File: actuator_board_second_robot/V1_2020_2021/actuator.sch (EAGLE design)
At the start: 26 parts, among them CON1 SM03B-GHS-TB, CON2 SM03B-GHS-TB, CON3 MOLEX_5566-2, U3 TCAN1042HVDR, U4 PCA9685PW, U5 TEENSY_3.1_BASIC_2

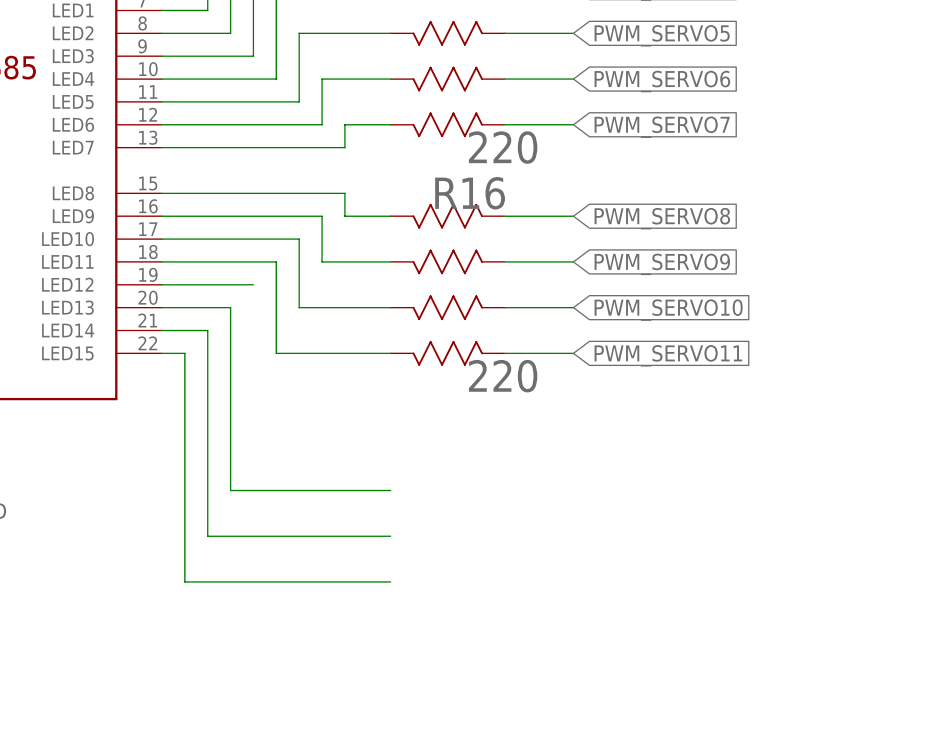
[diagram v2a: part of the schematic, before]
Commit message: Routed some airwires, removed fixed network resistor.
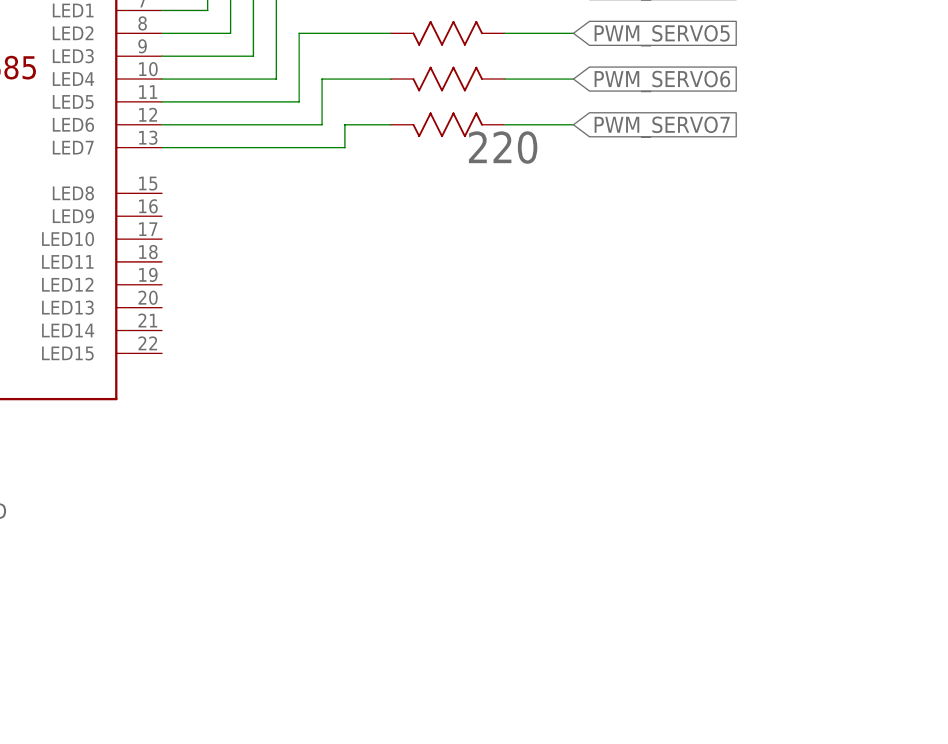
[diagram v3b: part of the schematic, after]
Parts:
- removed R16: 220, ARVP:EXB-V8V221JVEXBV8V-M
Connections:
- removed net N$1: U4.LED12
- removed net PWM_CH10: R16.66, U4.LED10
- removed net PWM_CH11: R16.58, U4.LED11
- removed net PWM_CH13: U4.LED13
- removed net PWM_CH14: U4.LED14
- removed net PWM_CH15: U4.LED15
- removed net PWM_CH8: R16.82, U4.LED8
- removed net PWM_CH9: R16.74, U4.LED9
- removed net PWM_SERVO10: R16.35
- removed net PWM_SERVO11: R16.47
- removed net PWM_SERVO8: R16.11
- removed net PWM_SERVO9: R16.23
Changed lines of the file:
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@@
 <part name="R14" library="ARVP" deviceset="EXB-V8V221JV" device="EXBV8V-M" value="220"/>
 <part name="R15" library="ARVP" deviceset="EXB-V8V221JV" device="EXBV8V-M" value="220"/>
-<part name="R16" library="ARVP" deviceset="EXB-V8V221JV" device="EXBV8V-M" value="220"/>
 <part name="R26" library="ARVP" deviceset="EXB-V8V221JV" device="EXBV8V-M" value="10k"/>
 <part name="SUPPLY10" library="supply2" library_urn="urn:adsk.eagle:library:372" deviceset="GND" device=""/>
@@
 <attribute name="NAME" x="147.5994" y="224.3328" size="3.4798" layer="95" ratio="10" rot="SMR0"/>
 </instance>
-<instance part="R16" gate="A" x="147.32" y="198.12" smashed="yes" rot="MR0">
-<attribute name="VALUE" x="151.2062" y="178.6128" size="3.4798" layer="96" ratio="10" rot="SMR0"/>
-<attribute name="NAME" x="147.5994" y="198.9328" size="3.4798" layer="95" ratio="10" rot="SMR0"/>
-</instance>
 <instance part="R26" gate="A" x="22.86" y="147.32" smashed="yes" rot="R90">
 <attribute name="NAME" x="22.0472" y="147.0406" size="3.4798" layer="95" ratio="10" rot="SR90"/>
@@
 </segment>
 </net>
-<net name="PWM_CH8" class="0">
-<segment>
-<pinref part="U4" gate="G$1" pin="LED8"/>
-<wire x1="109.22" y1="200.66" x2="129.54" y2="200.66" width="0.1524" layer="91"/>
-<wire x1="129.54" y1="200.66" x2="129.54" y2="198.12" width="0.1524" layer="91"/>
-<pinref part="R16" gate="A" pin="82"/>
-<wire x1="129.54" y1="198.12" x2="134.62" y2="198.12" width="0.1524" layer="91"/>
-</segment>
-</net>
-<net name="PWM_CH9" class="0">
-<segment>
-<pinref part="U4" gate="G$1" pin="LED9"/>
-<wire x1="109.22" y1="198.12" x2="127" y2="198.12" width="0.1524" layer="91"/>
-<wire x1="127" y1="198.12" x2="127" y2="193.04" width="0.1524" layer="91"/>
-<wire x1="127" y1="193.04" x2="134.62" y2="193.04" width="0.1524" layer="91"/>
-<pinref part="R16" gate="A" pin="74"/>
-</segment>
-</net>
-<net name="PWM_CH10" class="0">
-<segment>
-<wire x1="124.46" y1="187.96" x2="124.46" y2="195.58" width="0.1524" layer="91"/>
-<pinref part="U4" gate="G$1" pin="LED10"/>
-<wire x1="124.46" y1="195.58" x2="109.22" y2="195.58" width="0.1524" layer="91"/>
-<pinref part="R16" gate="A" pin="66"/>
-<wire x1="124.46" y1="187.96" x2="134.62" y2="187.96" width="0.1524" layer="91"/>
-</segment>
-</net>
-<net name="PWM_CH11" class="0">
-<segment>
-<pinref part="U4" gate="G$1" pin="LED11"/>
-<wire x1="109.22" y1="193.04" x2="121.92" y2="193.04" width="0.1524" layer="91"/>
-<wire x1="121.92" y1="193.04" x2="121.92" y2="182.88" width="0.1524" layer="91"/>
-<pinref part="R16" gate="A" pin="58"/>
-<wire x1="121.92" y1="182.88" x2="134.62" y2="182.88" width="0.1524" layer="91"/>
-</segment>
-</net>
-<net name="PWM_CH13" class="0">
-<segment>
-<wire x1="116.84" y1="167.64" x2="116.84" y2="187.96" width="0.1524" layer="91"/>
-<pinref part="U4" gate="G$1" pin="LED13"/>
-<wire x1="116.84" y1="187.96" x2="109.22" y2="187.96" width="0.1524" layer="91"/>
-<wire x1="116.84" y1="167.64" x2="134.62" y2="167.64" width="0.1524" layer="91"/>
-</segment>
-</net>
-<net name="PWM_CH14" class="0">
-<segment>
-<pinref part="U4" gate="G$1" pin="LED14"/>
-<wire x1="109.22" y1="185.42" x2="114.3" y2="185.42" width="0.1524" layer="91"/>
-<wire x1="114.3" y1="185.42" x2="114.3" y2="162.56" width="0.1524" layer="91"/>
-<wire x1="114.3" y1="162.56" x2="134.62" y2="162.56" width="0.1524" layer="91"/>
-</segment>
-</net>
-<net name="PWM_CH15" class="0">
-<segment>
-<wire x1="111.76" y1="157.48" x2="111.76" y2="182.88" width="0.1524" layer="91"/>
-<pinref part="U4" gate="G$1" pin="LED15"/>
-<wire x1="111.76" y1="182.88" x2="109.22" y2="182.88" width="0.1524" layer="91"/>
-<wire x1="111.76" y1="157.48" x2="134.62" y2="157.48" width="0.1524" layer="91"/>
-</segment>
-</net>
 <net name="PWM_SERVO0" class="0">
 <segment>
@@
 <wire x1="274.32" y1="246.38" x2="274.32" y2="251.46" width="0.1524" layer="91"/>
 <label x="274.32" y="251.46" size="1.778" layer="95" rot="R90" xref="yes"/>
-</segment>
-</net>
-<net name="PWM_SERVO11" class="0">
-<segment>
-<pinref part="R16" gate="A" pin="47"/>
-<wire x1="147.32" y1="182.88" x2="154.94" y2="182.88" width="0.1524" layer="91"/>
-<label x="154.94" y="182.88" size="1.778" layer="95" xref="yes"/>
-</segment>
-</net>
-<net name="PWM_SERVO10" class="0">
-<segment>
-<pinref part="R16" gate="A" pin="35"/>
-<wire x1="147.32" y1="187.96" x2="154.94" y2="187.96" width="0.1524" layer="91"/>
-<label x="154.94" y="187.96" size="1.778" layer="95" xref="yes"/>
-</segment>
-</net>
-<net name="PWM_SERVO9" class="0">
-<segment>
-<pinref part="R16" gate="A" pin="23"/>
-<wire x1="147.32" y1="193.04" x2="154.94" y2="193.04" width="0.1524" layer="91"/>
-<label x="154.94" y="193.04" size="1.778" layer="95" xref="yes"/>
-</segment>
-</net>
-<net name="PWM_SERVO8" class="0">
-<segment>
-<pinref part="R16" gate="A" pin="11"/>
-<wire x1="147.32" y1="198.12" x2="154.94" y2="198.12" width="0.1524" layer="91"/>
-<label x="154.94" y="198.12" size="1.778" layer="95" xref="yes"/>
 </segment>
 </net>
@@
 </segment>
 </net>
-<net name="N$1" class="0">
-<segment>
-<pinref part="U4" gate="G$1" pin="LED12"/>
-<wire x1="119.38" y1="190.5" x2="109.22" y2="190.5" width="0.1524" layer="91"/>
-</segment>
-</net>
